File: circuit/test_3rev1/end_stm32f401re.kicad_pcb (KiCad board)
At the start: 2 copper layers, 61 x 88.9 mm, 63 parts, among them J2 USB_B_Micro, U1 MAX98357, U2 STM32F401RETx, U3 AMS1117-3.3, U4 MAX98357, U5 ESP-12E

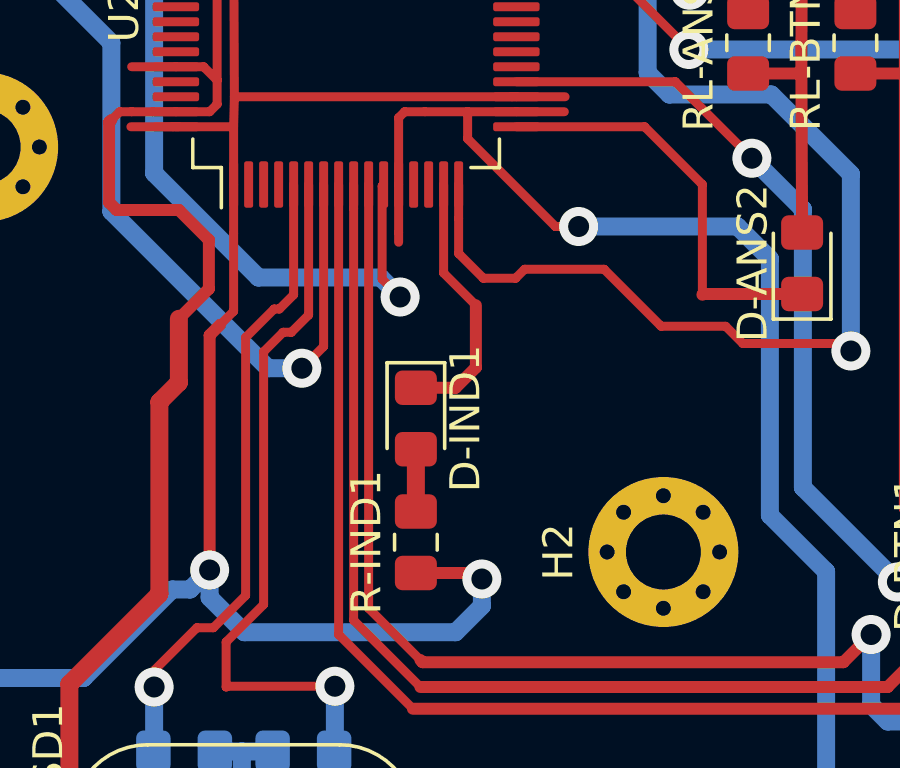
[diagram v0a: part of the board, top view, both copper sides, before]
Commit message: VREF (P13) need VDD
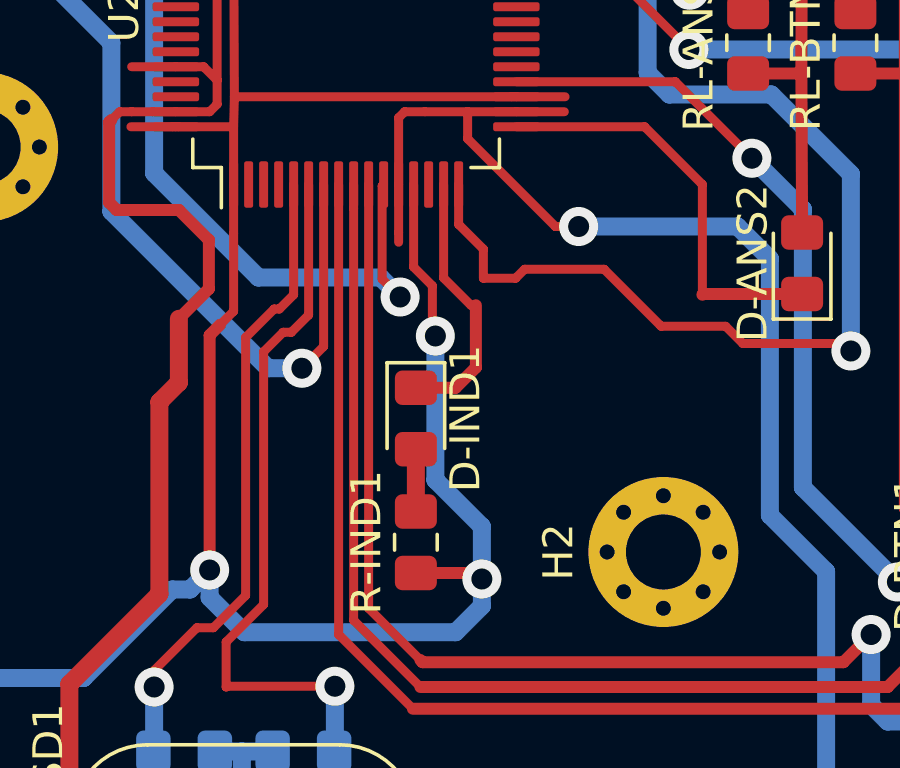
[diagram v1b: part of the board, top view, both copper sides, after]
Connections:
- U2 pad 13: Net-(U2-Pad13) -> VDD
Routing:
- net VDD: track 431.4 -> 445.5 mm, vias 16 -> 17

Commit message: Board revision
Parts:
- removed J-GAIN1: Conn_01x03_Male, Connector_PinHeader_2.00mm:PinHeader_1x03_P2.00mm_Vertical_SMD_Pin1Left
- added C-VCAP1: 4.7uF, Capacitor_Tantalum_SMD:CP_EIA-3216-18_Kemet-A, F.Cu at (89.4, 73.2)
- added D-LEDWIFI1: LED, LED_SMD:LED_0805_2012Metric_Pad1.15x1.40mm_HandSolder, F.Cu at (59.3, 45.4)
- added R-GAIN2: 100K, Resistor_SMD:R_0805_2012Metric_Pad1.15x1.40mm_HandSolder, F.Cu at (58.4, 70.5)
- added R-LEDWIFI1: 330, Resistor_SMD:R_0805_2012Metric_Pad1.15x1.40mm_HandSolder, F.Cu at (59.3, 43.2)
- added R-VDDESP1: 0, Resistor_SMD:R_0805_2012Metric_Pad1.15x1.40mm_HandSolder, B.Cu at (64.7, 57.2)
- C-SN1, C-SPL1, C-SPR1: value C -> 220pF
- moved R-GAIN1 4.03 mm to (55.3, 70.5), turned to 270 degrees
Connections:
- J-ESP-12E1 pad 1: VDD -> /VDD-ESP8266
- R-ESP12E1 pad 2: VDD -> /VDD-ESP8266
- R-ESP12E2 pad 2: VDD -> /VDD-ESP8266
- R-ESP12E3 pad 2: VDD -> /VDD-ESP8266
- R-ESP12E4 pad 2: VDD -> /VDD-ESP8266
- R-GAIN1 pad 2: Net-(J-GAIN1-Pad2) -> VDD
- U5 pad 5: Net-(U5-Pad5) -> /ESP_LEDWIFI
- U5 pad 8: VDD -> /VDD-ESP8266
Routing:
- net /VDD-ESP8266: track 0.00 -> 81.5 mm, vias 0 -> 2
- net VDD: track 445.5 -> 381.0 mm, vias 17 -> 14
- net /ESP_LEDWIFI: track 0.00 -> 11.1 mm, vias 0 -> 1
- net Net-(C-VCAP1-Pad1): track 0.00 -> 10.5 mm
- net GND: track 585.2 -> 592.8 mm
- net /DAC_GAIN: track 41.0 -> 47.1 mm
- net /LED_IND: track 8.92 -> 14.0 mm
- net Net-(J-GAIN1-Pad2): track 3.51 -> 0.00 mm
- net Net-(D-LEDWIFI1-Pad2): track 0.00 -> 2.21 mm

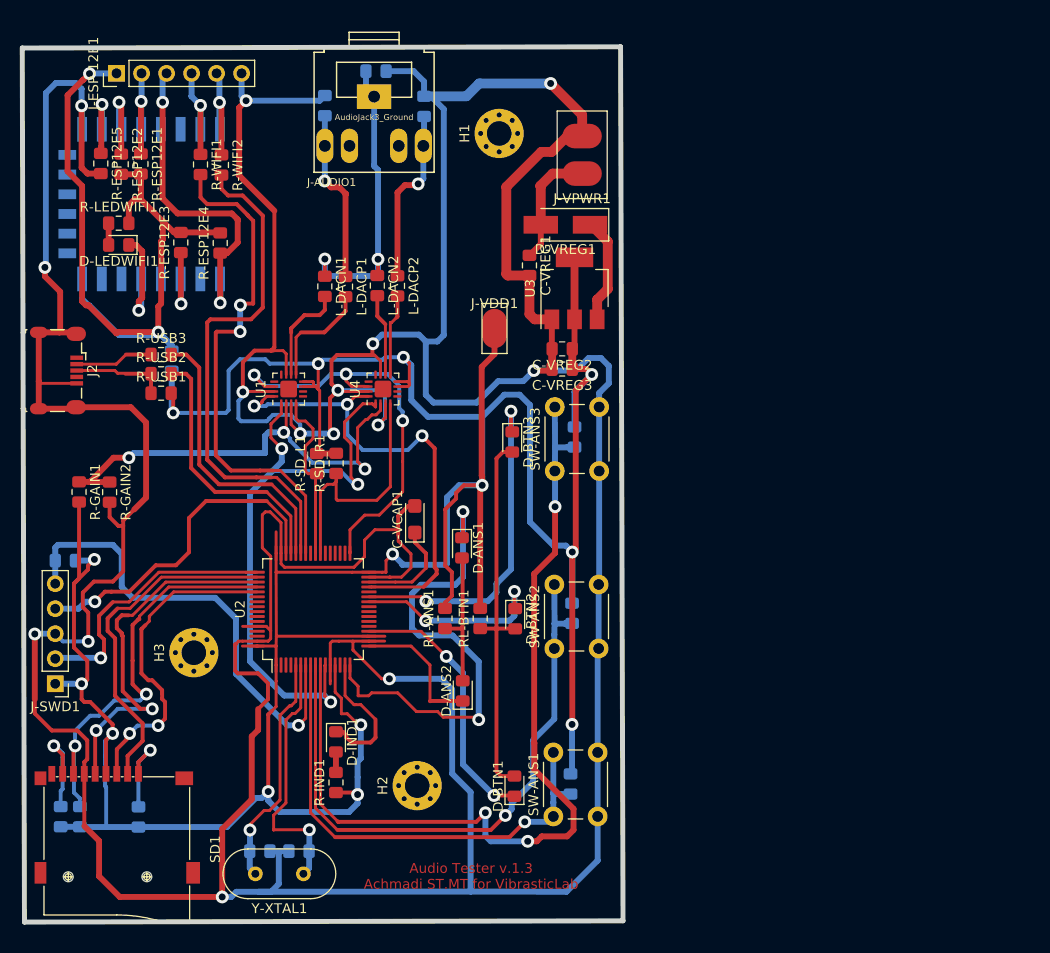
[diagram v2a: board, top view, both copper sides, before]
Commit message: add teardrop
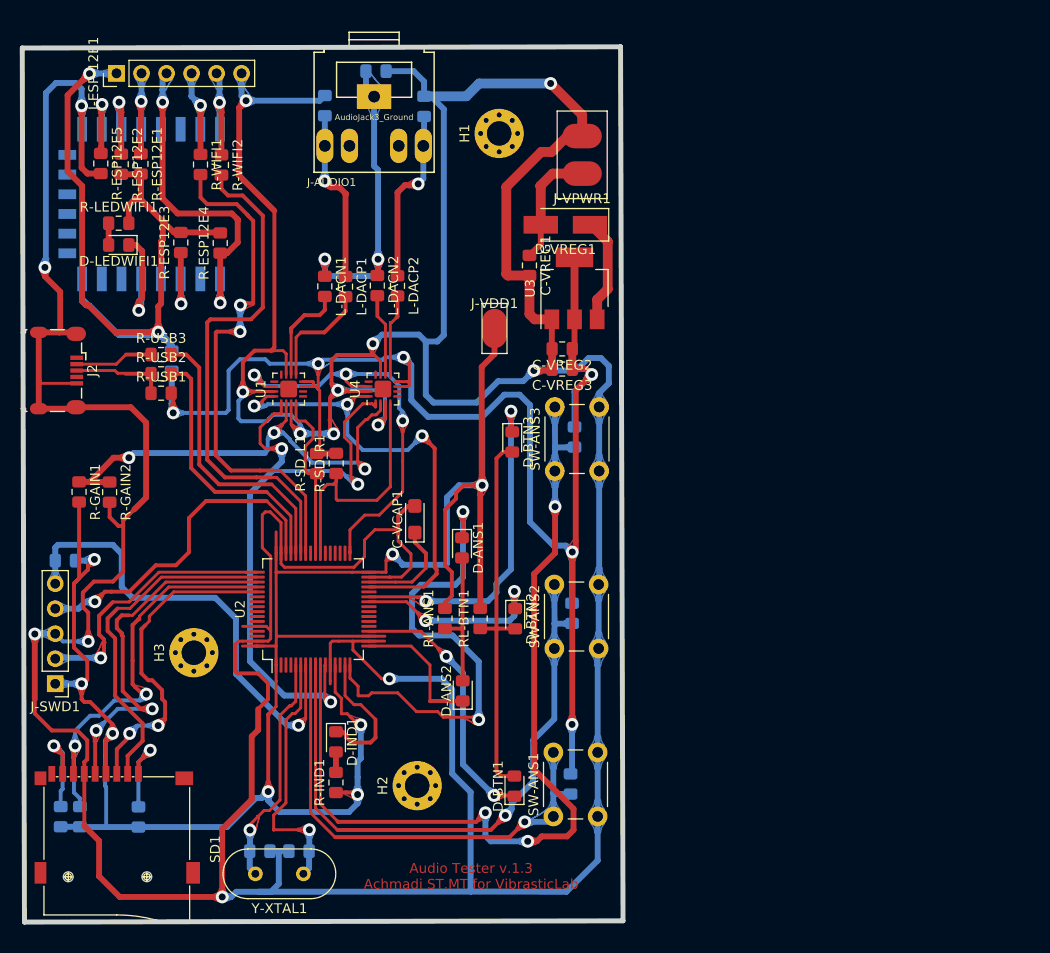
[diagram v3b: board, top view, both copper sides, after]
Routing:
- net /DAC_DIN: track 63.4 -> 65.8 mm

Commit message: update PCB
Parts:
- L-DACN1, L-DACN2, L-DACP1, L-DACP2: value L -> 100uH
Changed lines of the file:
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@@
   )
   (setup
-    (last_trace_width 0.3)
+    (last_trace_width 0.25)
     (user_trace_width 0.3)
     (user_trace_width 0.4)
@@
       (effects (font (size 1 1) (thickness 0.15)))
     )
-    (fp_text value L (at 0 1.65 90) (layer F.Fab)
+    (fp_text value 100uH (at 0 1.65 90) (layer F.Fab)
       (effects (font (size 1 1) (thickness 0.15)))
     )
@@
       (effects (font (size 1 1) (thickness 0.15)))
     )
-    (fp_text value L (at 0 1.65 90) (layer F.Fab)
+    (fp_text value 100uH (at 0 1.65 90) (layer F.Fab)
       (effects (font (size 1 1) (thickness 0.15)))
     )
@@
       (effects (font (size 1 1) (thickness 0.15)))
     )
-    (fp_text value L (at 0 1.65 90) (layer F.Fab)
+    (fp_text value 100uH (at 0 1.65 90) (layer F.Fab)
       (effects (font (size 1 1) (thickness 0.15)))
     )
@@
       (effects (font (size 1 1) (thickness 0.15)))
     )
-    (fp_text value L (at 0 1.65 90) (layer F.Fab)
-      (effects (font (size 1 1) (thickness 0.15)))
-    )
+    (fp_text value 100uH (at 0 1.65 90) (layer F.Fab)
+      (effects (font (size 1 1) (thickness 0.15)))
+    )

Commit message: reset button
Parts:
- added SW-RST1: SW_Push, Button_Switch_THT:SW_PUSH_6mm, F.Cu at (84.2, 108.0)
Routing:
- net /NRST: track 47.8 -> 98.3 mm, vias 1 -> 3
- net GND: track 592.8 -> 607.6 mm
- net /BTN_C: track 91.5 -> 90.8 mm
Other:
- board size 61 x 88.9 mm -> 61 x 89.7 mm
- board text removed: "Audio Tester v.1.3 Achmadi ST.MT for VibrasticLab"

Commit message: new PCB
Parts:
- removed G***: LOGO, viblab:viblab
- added H4: MountingHole, MountingHole:MountingHole_2.5mm_Pad_Via, F.Cu at (143.3, 38.1)
- added H5: CableHole, MountingHole:MountingHole_2.5mm_Pad_Via, F.Cu at (58.0, 30.4)
- added U6: SPH0645, mic:sph0645, F.Cu at (67.3, 82.3)
- D-ANS1, D-ANS2, D-BTN1, D-BTN2, D-BTN3, D-IND1, D-LEDWIFI1: footprint LED_SMD:LED_0805_2012Metric_Pad1.15x1.40mm_HandSolder -> LED_SMD:LED_1206_3216Metric_Pad1.42x1.75mm_HandSolder
- R-GAIN1, R-GAIN2, R-IND1, RL-ANS1, RL-BTN1: moved to B.Cu
- R-VDDESP1: moved to F.Cu
- moved SD1 88.1 mm to (144.2, 84.0), turned to 0 degrees
- moved R-SD3 87.6 mm to (139.9, 89.8), turned to 0 degrees
- moved R-SD2 86.0 mm to (139.9, 87.8), turned to 0 degrees
- moved C-XTAL1 82.4 mm to (145.8, 67.3), turned to 90 degrees
- moved R-SD1 81.5 mm to (139.9, 81.9), turned to 0 degrees
- moved C-XTAL2 81.1 mm to (145.8, 63.2), turned to 270 degrees
- moved Y-XTAL1 80.2 mm to (143.4, 62.9), turned to 270 degrees
- moved SW-ANS1 76.3 mm to (133.7, 33.4), turned to 180 degrees
- moved SW-RST1 74.9 mm to (138.7, 56.6), turned to 90 degrees
- moved J-SWD1 74.4 mm to (127.2, 92.2), turned to 270 degrees
- moved R-ANS1 73.6 mm to (130.3, 31.0), turned to 180 degrees
- moved D-BTN1 70.8 mm to (130.2, 36.6), turned to 0 degrees
- moved R-IND1 65.6 mm to (130.0, 56.0), turned to 0 degrees
- moved D-IND1 62.8 mm to (129.9, 56.0), turned to 0 degrees
- moved H3 62.5 mm to (127.8, 73.0)
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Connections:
- U5 pad 20: Net-(U5-Pad20) -> /ESP_LEDWIFI
- U5 pad 5: /ESP_LEDWIFI -> /MIC_LRCL
- U5 pad 6: Net-(U5-Pad6) -> /MIC_DOUT
- U5 pad 7: Net-(U5-Pad7) -> /MIC_BCLK
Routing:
- net VDD: track 381.0 -> 461.5 mm, vias 14 -> 19
- net GND: track 607.6 -> 535.1 mm, vias 15 -> 14
- net /MIC_LRCL: track 0.00 -> 44.1 mm
- net /MIC_DOUT: track 0.00 -> 35.1 mm
- net /ESP_RST: track 35.4 -> 68.8 mm, vias 2 -> 5
- net /MIC_BCLK: track 0.00 -> 26.6 mm
- net /DAC_DIN: track 65.8 -> 91.0 mm
- net /WIFI_TXD: track 52.8 -> 76.4 mm
- net Net-(D-ANS1-Pad2): track 14.3 -> 36.6 mm, vias 0 -> 3
- net /WIFI_RXD: track 52.8 -> 74.6 mm, vias 0 -> 2
- net Net-(L-DACP1-Pad2): track 11.4 -> 28.0 mm
- net Net-(L-DACN1-Pad2): track 10.3 -> 26.6 mm
- net Net-(L-DACP2-Pad2): track 8.36 -> 24.5 mm
- net Net-(L-DACN2-Pad2): track 8.35 -> 23.7 mm
- net /MMC_MOSI: track 32.8 -> 44.5 mm
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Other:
- board size 61 x 89.7 mm -> 98.9 x 72.2 mm
